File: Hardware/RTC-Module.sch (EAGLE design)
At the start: 26 parts, among them J1 SMD, J2 SMD, J3 PTH, U2 RV-1805

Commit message: laying out with battery
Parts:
- removed U$3, U$5: SPARKX-LOGO4, SparkX:SPARKX-LOGO4
- added BT1: (no value), SparkFun-Batteries:BATTERY-12MM_PTH
- added JP1: JUMPER-SMT_3_1-NC_TRACE_NO-SILK, SparkFun-Jumpers:JUMPER-SMT_3_1-NC_TRACE_NO-SILK
- added R5: 470, SparkFun-Resistors:470OHM-0603-1/10W-1%
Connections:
- new net N$3: BT1.+, R5.1
- new net N$6: C1.+, JP1.3
- new net N$7: JP1.1, R5.2
- net GND: now also BT1.-
- net N$5: now also JP1.2; no longer C1.+
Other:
- note added: "Cut trace on jumper JP1 to disconnect SuperCapacitor. Add solder to other side of jumper to connect optional battery"
- moved on the sheet: C1, C3, R6
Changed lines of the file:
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@@
 <part name="SUPPLY4" library="SparkFun-PowerSymbols" deviceset="3.3V" device=""/>
 <part name="C1" library="SparkFun-Capacitors" deviceset=".22F-SUPERCAP" device=""/>
-<part name="U$3" library="SparkX" deviceset="SPARKX-LOGO" device="4" value="SPARKX-LOGO4"/>
-<part name="U$5" library="SparkX" deviceset="SPARKX-LOGO" device="4"/>
 <part name="U2" library="SparkFun-Clocks" deviceset="RV-1805" device=""/>
 <part name="GND1" library="SparkFun" deviceset="GND" device=""/>
@@
 <part name="J4" library="SparkFun-Connectors" deviceset="CONN_03" device="1X03_NO_SILK"/>
 <part name="GND4" library="SparkFun" deviceset="GND" device=""/>
+<part name="BT1" library="SparkFun-Batteries" deviceset="BATTERY" device="-12MM_PTH"/>
+<part name="R5" library="SparkFun-Resistors" deviceset="470OHM" device="-0603-1/10W-1%" value="470"/>
+<part name="GND8" library="SparkFun" deviceset="GND" device=""/>
+<part name="JP1" library="SparkFun-Jumpers" deviceset="JUMPER-SMT_3_1-NC_TRACE" device="_NO-SILK"/>
 </parts>
 <sheets>
@@
 <text x="165.1" y="149.86" size="2.54" layer="97" font="vector">RTC Module</text>
 <text x="38.1" y="48.26" size="2.54" layer="97" font="vector">Qwiic Connectors/ I2C Interface</text>
+<text x="15.24" y="106.68" size="1.778" layer="97">Cut trace on jumper JP1
+to disconnect SuperCapacitor.
+Add solder to other side of
+jumper to connect optional
+battery</text>
 </plain>
 <instances>
 <instance part="U$6" gate="G$1" x="238.76" y="27.94"/>
 <instance part="U$7" gate="G$1" x="241.3" y="27.94"/>
-<instance part="GND2" gate="1" x="53.34" y="109.22"/>
+<instance part="GND2" gate="1" x="53.34" y="91.44"/>
 <instance part="R1" gate="G$1" x="175.26" y="124.46" rot="R90"/>
 <instance part="R2" gate="G$1" x="190.5" y="124.46" rot="R90"/>
@@
 <instance part="GND7" gate="1" x="93.98" y="22.86"/>
 <instance part="SUPPLY4" gate="G$1" x="93.98" y="38.1"/>
-<instance part="C1" gate="G$1" x="53.34" y="119.38"/>
-<instance part="U$3" gate="G$1" x="200.66" y="40.64"/>
-<instance part="U$5" gate="G$1" x="200.66" y="40.64"/>
+<instance part="C1" gate="G$1" x="53.34" y="101.6" smashed="yes">
+<attribute name="NAME" x="54.356" y="102.235" size="1.778" layer="95" font="vector"/>
+<attribute name="VALUE" x="49.911" y="84.836" size="1.778" layer="96" font="vector" rot="R90"/>
+</instance>
 <instance part="U2" gate="U1" x="160.02" y="106.68"/>
 <instance part="GND1" gate="1" x="137.16" y="93.98"/>
@@
 <instance part="C2" gate="G$1" x="137.16" y="101.6"/>
 <instance part="SUPPLY8" gate="G$1" x="144.78" y="119.38"/>
-<instance part="C3" gate="G$1" x="81.28" y="116.84"/>
+<instance part="C3" gate="G$1" x="78.74" y="119.38"/>
 <instance part="C4" gate="G$1" x="121.92" y="101.6"/>
-<instance part="R6" gate="G$1" x="53.34" y="129.54" rot="R90"/>
-<instance part="GND9" gate="1" x="81.28" y="109.22"/>
+<instance part="R6" gate="G$1" x="60.96" y="119.38" rot="R90"/>
+<instance part="GND9" gate="1" x="78.74" y="111.76"/>
 <instance part="SUPPLY1" gate="G$1" x="121.92" y="109.22"/>
 <instance part="GND10" gate="1" x="121.92" y="93.98"/>
@@
 <instance part="J4" gate="J$1" x="109.22" y="33.02"/>
 <instance part="GND4" gate="1" x="144.78" y="93.98"/>
+<instance part="BT1" gate="G$1" x="68.58" y="86.36" rot="R270"/>
+<instance part="R5" gate="G$1" x="68.58" y="99.06" rot="R90"/>
+<instance part="GND8" gate="1" x="68.58" y="76.2"/>
+<instance part="JP1" gate="G$1" x="60.96" y="106.68" smashed="yes" rot="R270">
+<attribute name="NAME" x="60.96" y="110.109" size="1.778" layer="95" font="vector" rot="R180"/>
+</instance>
 </instances>
 <busses>
@@
 <pinref part="C1" gate="G$1" pin="-"/>
 <pinref part="GND2" gate="1" pin="GND"/>
-<wire x1="53.34" y1="114.3" x2="53.34" y2="111.76" width="0.1524" layer="91"/>
+<wire x1="53.34" y1="96.52" x2="53.34" y2="93.98" width="0.1524" layer="91"/>
 </segment>
 <segment>
@@
 <segment>
 <pinref part="C3" gate="G$1" pin="2"/>
-<wire x1="81.28" y1="114.3" x2="81.28" y2="111.76" width="0.1524" layer="91"/>
+<wire x1="78.74" y1="116.84" x2="78.74" y2="114.3" width="0.1524" layer="91"/>
 <pinref part="GND9" gate="1" pin="GND"/>
 </segment>
@@
 <pinref part="GND4" gate="1" pin="GND"/>
 <wire x1="144.78" y1="96.52" x2="144.78" y2="99.06" width="0.1524" layer="91"/>
+</segment>
+<segment>
+<pinref part="BT1" gate="G$1" pin="-"/>
+<pinref part="GND8" gate="1" pin="GND"/>
+<wire x1="68.58" y1="78.74" x2="68.58" y2="81.28" width="0.1524" layer="91"/>
 </segment>
 </net>
@@
 <net name="VBACKUP" class="0">
 <segment>
-<label x="55.88" y="137.16" size="1.27" layer="95" font="vector" xref="yes"/>
-<wire x1="53.34" y1="137.16" x2="55.88" y2="137.16" width="0.1524" layer="91"/>
+<label x="83.82" y="127" size="1.27" layer="95" font="vector" xref="yes"/>
+<wire x1="78.74" y1="127" x2="83.82" y2="127" width="0.1524" layer="91"/>
+<pinref part="C3" gate="G$1" pin="1"/>
+<wire x1="78.74" y1="127" x2="78.74" y2="124.46" width="0.1524" layer="91"/>
 <pinref part="R6" gate="G$1" pin="2"/>
-<wire x1="53.34" y1="137.16" x2="53.34" y2="134.62" width="0.1524" layer="91"/>
+<wire x1="60.96" y1="124.46" x2="60.96" y2="127" width="0.1524" layer="91"/>
+<wire x1="60.96" y1="127" x2="78.74" y2="127" width="0.1524" layer="91"/>
+<junction x="78.74" y="127"/>
 </segment>
 <segment>
@@
 <wire x1="147.32" y1="114.3" x2="144.78" y2="114.3" width="0.1524" layer="91"/>
 <label x="144.78" y="114.3" size="1.27" layer="95" font="vector" rot="R180" xref="yes"/>
-</segment>
-<segment>
-<pinref part="C3" gate="G$1" pin="1"/>
-<wire x1="81.28" y1="121.92" x2="81.28" y2="124.46" width="0.1524" layer="91"/>
-<wire x1="81.28" y1="124.46" x2="83.82" y2="124.46" width="0.1524" layer="91"/>
-<label x="83.82" y="124.46" size="1.27" layer="95" font="vector" xref="yes"/>
-</segment>
-</net>
-<net name="N$5" class="0">
-<segment>
-<pinref part="R6" gate="G$1" pin="1"/>
-<pinref part="C1" gate="G$1" pin="+"/>
-<wire x1="53.34" y1="121.92" x2="53.34" y2="124.46" width="0.1524" layer="91"/>
 </segment>
 </net>
@@
 </segment>
 </net>
+<net name="N$3" class="0">
+<segment>
+<pinref part="BT1" gate="G$1" pin="+"/>
+<pinref part="R5" gate="G$1" pin="1"/>
+<wire x1="68.58" y1="93.98" x2="68.58" y2="91.44" width="0.1524" layer="91"/>
+</segment>
+</net>
+<net name="N$5" class="0">
+<segment>
+<pinref part="JP1" gate="G$1" pin="2"/>
+<pinref part="R6" gate="G$1" pin="1"/>
+<wire x1="60.96" y1="114.3" x2="60.96" y2="111.76" width="0.1524" layer="91"/>
+</segment>
+</net>
+<net name="N$6" class="0">
+<segment>
+<pinref part="C1" gate="G$1" pin="+"/>
+<wire x1="53.34" y1="104.14" x2="53.34" y2="106.68" width="0.1524" layer="91"/>
+<pinref part="JP1" gate="G$1" pin="3"/>
+<wire x1="53.34" y1="106.68" x2="55.88" y2="106.68" width="0.1524" layer="91"/>
+</segment>
+</net>
+<net name="N$7" class="0">
+<segment>
+<pinref part="JP1" gate="G$1" pin="1"/>
+<pinref part="R5" gate="G$1" pin="2"/>
+<wire x1="66.04" y1="106.68" x2="68.58" y2="106.68" width="0.1524" layer="91"/>
+<wire x1="68.58" y1="106.68" x2="68.58" y2="104.14" width="0.1524" layer="91"/>
+</segment>
+</net>
 </nets>
 </sheet>
@@
 </schematic>
 </drawing>
+<compatibility>
+<note version="6.3" minversion="6.2.2" severity="warning">
+Since Version 6.2.2 text objects can contain more than one line,
+which will not be processed correctly with this version.
+</note>
+</compatibility>
 </eagle>

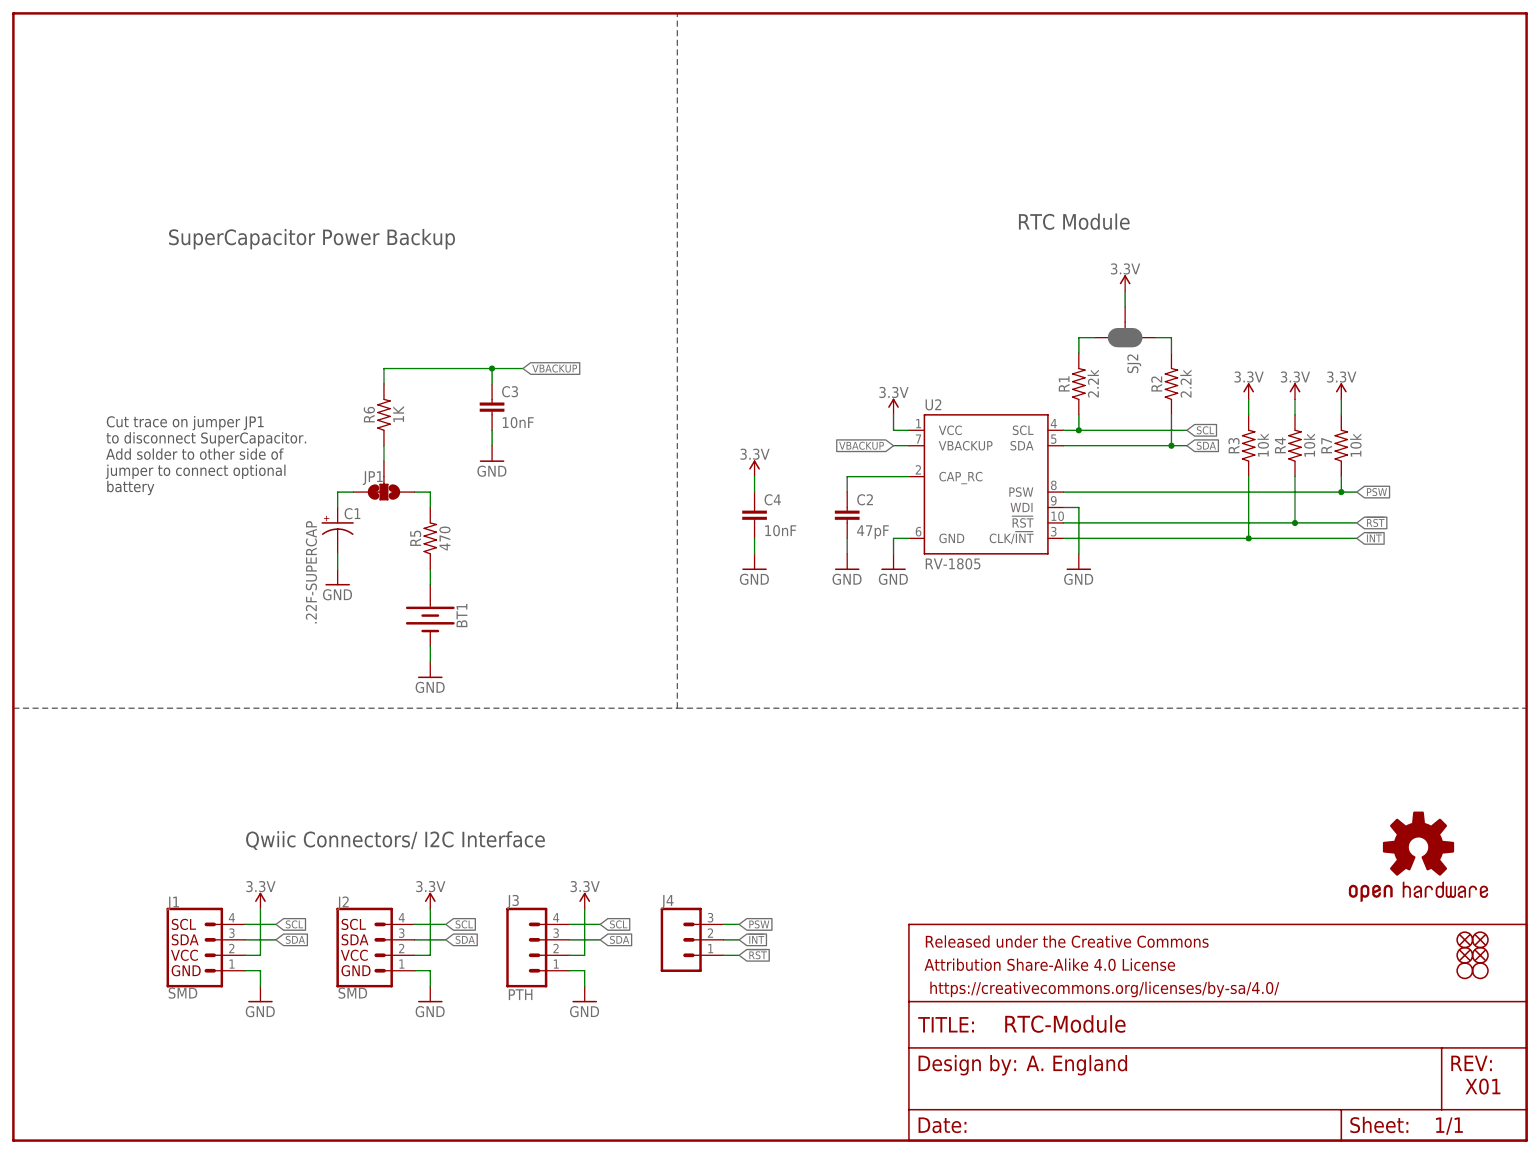
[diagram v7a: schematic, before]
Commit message: added battery footprint, went through engineering checklist
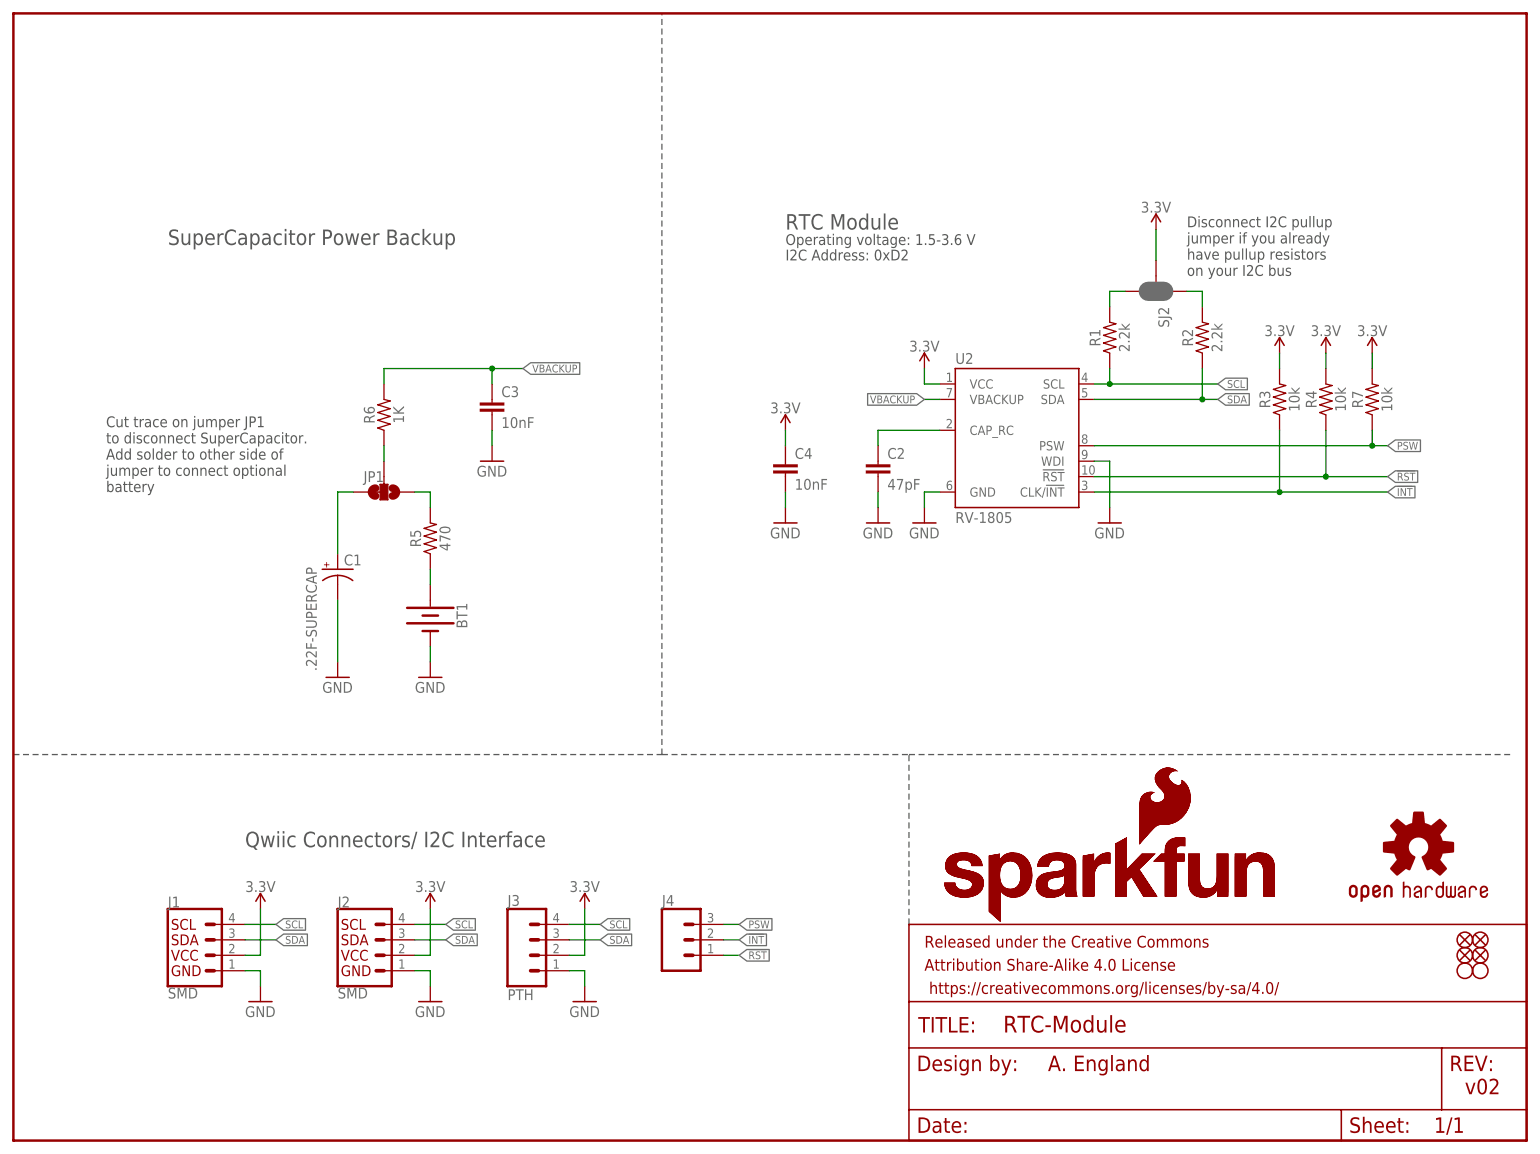
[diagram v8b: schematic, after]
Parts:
- added LOGO2, LOGO3: SFE_LOGO_NAME_FLAME.1_INCH, SparkFun-Aesthetics:SFE_LOGO_NAME_FLAME.1_INCH
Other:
- note added: "Disconnect I2C pullup jumper if you already have pullup resistors on your I2C bus"
- note added: "I2C Address: 0xD2"
- note added: "Operating voltage: 1.5-3.6 V"
- note added: "v02"
- note removed: "X01"
- moved on the sheet: C1, C2, C4, R1, R2, R3, R4, R7, SJ2, U2
